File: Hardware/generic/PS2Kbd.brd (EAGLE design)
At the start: 88.9 x 61.9 mm, 29 parts, among them CN3 AVR-ISP-6-DIP, IC1 MEGA16-P, IC2 MT8816P

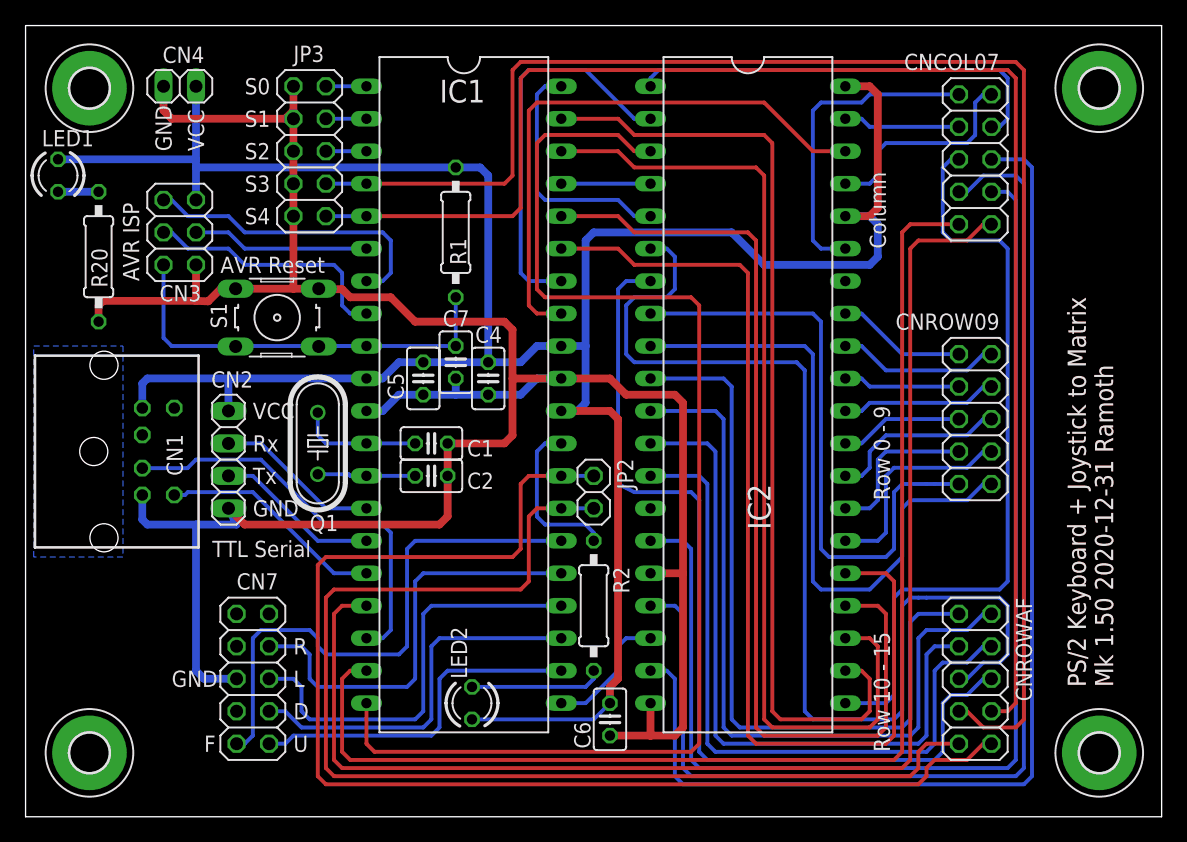
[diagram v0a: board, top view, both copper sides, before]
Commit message: Updated building docs. Revised generic board.
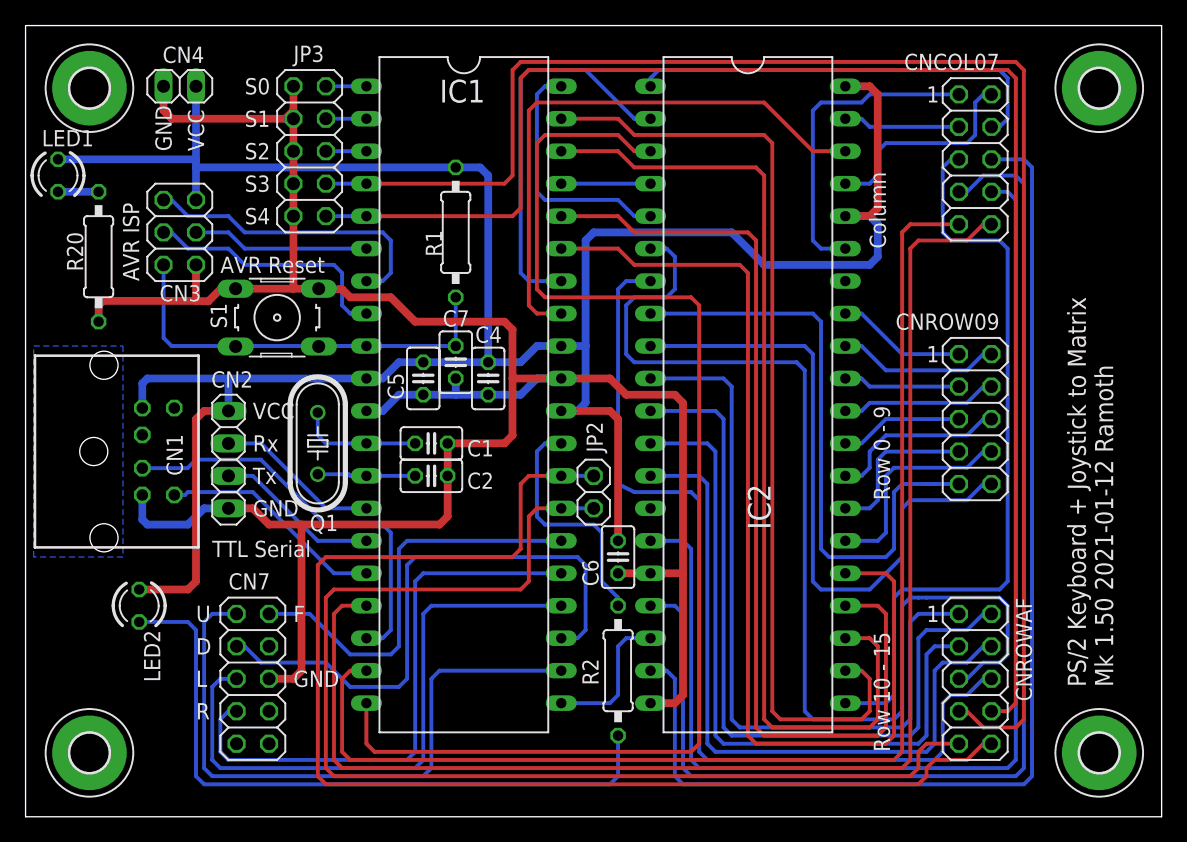
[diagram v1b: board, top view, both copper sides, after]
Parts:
- moved LED2 27.1 mm to (8.89, 16.5), turned to 270 degrees
- moved C6 12.7 mm to (46.4, 20.3)
- moved R2 5.43 mm to (46.4, 11.4)
- turned CN7 to 270 degrees
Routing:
- net N$1: track 10.4 -> 52.9 mm
- net JS_UP: track 27.5 -> 49.9 mm
- net JS_DN: track 29.6 -> 45.5 mm
- net JS_L: track 33.4 -> 47.4 mm
- net JS_R: track 33.4 -> 44.9 mm
- net JS_F: track 42.9 -> 32.3 mm
- net GND: track 197.9 -> 190.1 mm
- net JS_PROG: track 12.9 -> 19.1 mm
- net VCC: track 195.4 -> 191.4 mm
- net MT_STROBE: track 10.2 -> 11.3 mm
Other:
- board text added: "1"
- board text added: "PS/2 Keyboard + Joystick to Matrix Mk 1.50 2021-01-12 Ramoth"
- board text removed: "PS/2 Keyboard + Joystick to Matrix Mk 1.50 2020-12-31 Ramoth"

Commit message: Added separate tables for TRS80 Model 3 / Model 4 as the 3 doesn't have some of the keys the 4 has (CTRL, CAPS and 3 function keys).
Added pdf schematic and gerbers for Generic version of hardware.
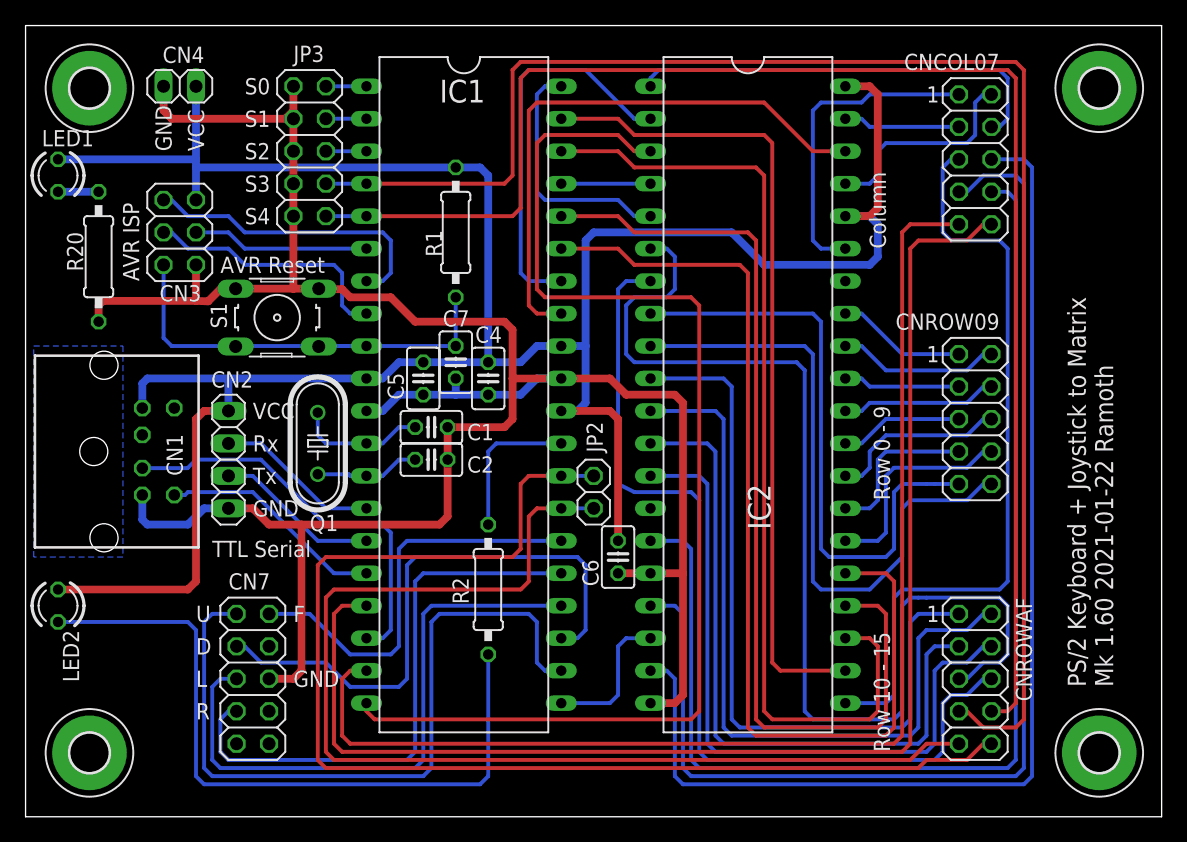
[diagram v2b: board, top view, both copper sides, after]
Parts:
- moved R2 12.0 mm to (36.2, 17.8)
- moved LED2 6.35 mm to (2.54, 16.5)
- moved C1 1.27 mm to (31.8, 30.5)
- moved C2 1.27 mm to (31.8, 27.9)
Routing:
- net MTX1: track 74.6 -> 63.9 mm
- net JS_UP: track 49.9 -> 58.1 mm
- net JS_PROG: track 19.1 -> 11.7 mm
- net VCC: track 191.4 -> 197.7 mm
- net MT_RESET: track 98.4 -> 93.3 mm
- net Y8-COL8: track 97.6 -> 95.0 mm
- net N$1: track 52.9 -> 55.4 mm
- net !TARGET_RESET: track 107.0 -> 104.4 mm
- net PC5: track 91.7 -> 89.2 mm
- net PC6: track 98.6 -> 96.5 mm
- net MTX2: track 77.1 -> 75.9 mm
- net MTY0: track 77.1 -> 75.9 mm
- net MTY1: track 79.7 -> 78.4 mm
- net N$3: track 7.67 -> 8.20 mm
- net N$2: track 9.66 -> 10.2 mm
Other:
- board text added: "PS/2 Keyboard + Joystick to Matrix Mk 1.60 2021-01-22 Ramoth"
- board text removed: "PS/2 Keyboard + Joystick to Matrix Mk 1.50 2021-01-12 Ramoth"
